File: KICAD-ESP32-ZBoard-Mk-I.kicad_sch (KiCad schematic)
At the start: 33 parts, among them J1 DC_Jack, J10 USB_A, J2 Conn_01x03_Pin-RAIL_1, J3 Conn_01x02_Pin-RAIL_1, J4 Conn_01x03_Pin-RAIL_2, J5 Conn_01x02_Pin-RAIL_2, J6 Conn_01x03_Pin-RAIL_3, J7 Conn_01x02_Pin-RAIL_3, J8 Conn_01x13_Pin-LEFT, J9 Conn_01x13_Pin-RIGHT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

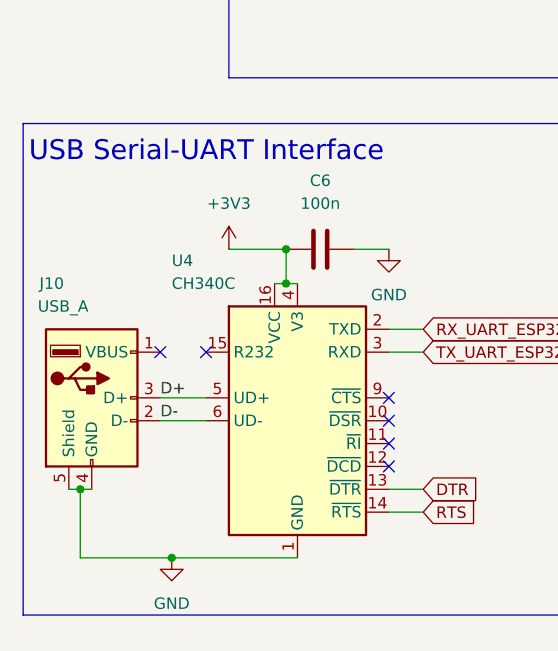
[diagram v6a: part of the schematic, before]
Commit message: ADDED all remaining pin labels. ADDED serial-breakout pins in case alternative USB is wanted.
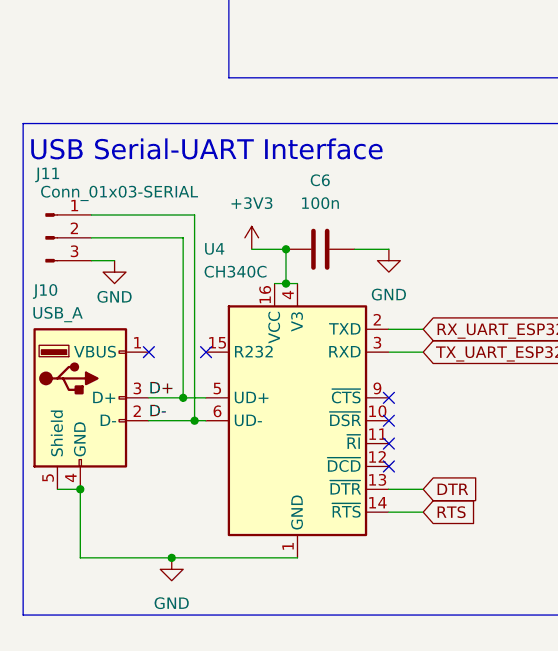
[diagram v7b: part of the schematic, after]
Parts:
- added J11: Conn_01x03-SERIAL, Connector_PinHeader_2.54mm:PinHeader_1x03_P2.54mm_Vertical, symbol Connector:Conn_01x03_Pin
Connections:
- net D+: now also J11.2 (Pin_2)
- net D-: now also J11.1 (Pin_1)
- net GND: now also J11.3 (Pin_3)
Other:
- moved on the sheet: J10
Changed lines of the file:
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@@
 	)
 	(junction
+		(at 34.29 151.13)
+		(diameter 0)
+		(color 0 0 0 0)
+	)
+	(junction
 		(at 66.04 87.63)
 		(diameter 0)
@@
 	)
 	(junction
+		(at 33.02 148.59)
+		(diameter 0)
+		(color 0 0 0 0)
+	)
+	(junction
 		(at 134.62 39.37)
 		(diameter 0)
@@
 	)
 	(no_connect
-		(at 30.48 143.51)
+		(at 29.21 143.51)
 	)
 	(no_connect
@@
 	(wire
 		(pts
-			(xy 21.59 158.75) (xy 20.32 158.75)
+			(xy 21.59 158.75) (xy 19.05 158.75)
 		)
 		(stroke
@@
 	(wire
 		(pts
+			(xy 29.21 151.13) (xy 34.29 151.13)
+		)
+		(stroke
+			(width 0)
+			(type default)
+		)
+	)
+	(wire
+		(pts
 			(xy 154.94 156.21) (xy 158.75 156.21)
 		)
@@
 	(wire
 		(pts
+			(xy 22.86 130.81) (xy 33.02 130.81)
+		)
+		(stroke
+			(width 0)
+			(type default)
+		)
+	)
+	(wire
+		(pts
 			(xy 186.69 158.75) (xy 190.5 158.75)
 		)
@@
 	(wire
 		(pts
-			(xy 93.98 33.02) (xy 105.41 33.02)
+			(xy 34.29 128.27) (xy 34.29 151.13)
 		)
 		(stroke
@@
 	(wire
 		(pts
-			(xy 30.48 151.13) (xy 35.56 151.13)
+			(xy 93.98 33.02) (xy 105.41 33.02)
 		)
 		(stroke
@@
 	(wire
 		(pts
-			(xy 38.1 132.08) (xy 44.45 132.08)
+			(xy 40.64 132.08) (xy 44.45 132.08)
 		)
 		(stroke
@@
 	(wire
 		(pts
-			(xy 22.86 158.75) (xy 21.59 158.75)
-		)
-		(stroke
-			(width 0)
-			(type default)
-		)
-	)
-	(wire
-		(pts
 			(xy 95.25 137.16) (xy 96.52 137.16)
 		)
@@
 	(wire
 		(pts
-			(xy 30.48 148.59) (xy 35.56 148.59)
+			(xy 29.21 148.59) (xy 33.02 148.59)
 		)
 		(stroke
@@
 	(wire
 		(pts
+			(xy 33.02 148.59) (xy 35.56 148.59)
+		)
+		(stroke
+			(width 0)
+			(type default)
+		)
+	)
+	(wire
+		(pts
 			(xy 52.07 132.08) (xy 55.88 132.08)
 		)
@@
 	(wire
 		(pts
+			(xy 34.29 151.13) (xy 35.56 151.13)
+		)
+		(stroke
+			(width 0)
+			(type default)
+		)
+	)
+	(wire
+		(pts
 			(xy 154.94 135.89) (xy 158.75 135.89)
 		)
@@
 	(wire
 		(pts
+			(xy 33.02 130.81) (xy 33.02 148.59)
+		)
+		(stroke
+			(width 0)
+			(type default)
+		)
+	)
+	(wire
+		(pts
 			(xy 186.69 161.29) (xy 190.5 161.29)
 		)
@@
 	(wire
 		(pts
+			(xy 22.86 128.27) (xy 34.29 128.27)
+		)
+		(stroke
+			(width 0)
+			(type default)
+		)
+	)
+	(wire
+		(pts
 			(xy 39.37 36.83) (xy 39.37 33.02)
 		)
@@
 	(wire
 		(pts
+			(xy 22.86 133.35) (xy 25.4 133.35)
+		)
+		(stroke
+			(width 0)
+			(type default)
+		)
+	)
+	(wire
+		(pts
 			(xy 66.04 99.06) (xy 58.42 99.06)
 		)
@@
 	)
 	(label "D-"
-		(at 30.48 151.13 0)
+		(at 29.21 151.13 0)
 		(effects
 			(font
@@
 	)
 	(label "D+"
-		(at 30.48 148.59 0)
+		(at 29.21 148.59 0)
 		(effects
 			(font
@@
 	(symbol
 		(lib_id "power:+3V3")
-		(at 38.1 132.08 0)
+		(at 40.64 132.08 0)
 		(unit 1)
 		(exclude_from_sim no)
@@
 		(fields_autoplaced yes)
 		(property "Reference" "#PWR013"
-			(at 38.1 135.89 0)
+			(at 40.64 135.89 0)
 			(effects
 				(font
@@
 		)
 		(property "Value" "+3V3"
-			(at 38.1 127 0)
+			(at 40.64 127 0)
 			(effects
 				(font
@@
 		)
 		(property "Footprint" ""
-			(at 38.1 132.08 0)
+			(at 40.64 132.08 0)
 			(effects
 				(font
@@
 		)
 		(property "Datasheet" ""
-			(at 38.1 132.08 0)
+			(at 40.64 132.08 0)
 			(effects
 				(font
@@
 		)
 		(property "Description" "Power symbol creates a global label with name \"+3V3\""
-			(at 38.1 132.08 0)
+			(at 40.64 132.08 0)
 			(effects
 				(font
@@
 	(symbol
 		(lib_id "Connector:Conn_01x03_Pin")
+		(at 17.78 130.81 0)
+		(unit 1)
+		(exclude_from_sim no)
+		(in_bom yes)
+		(on_board yes)
+		(dnp no)
+		(property "Reference" "J11"
+			(at 18.034 123.698 0)
+			(effects
+				(font
+					(size 1.27 1.27)
+				)
+			)
+		)
+		(property "Value" "Conn_01x03-SERIAL"
+			(at 25.908 125.73 0)
+			(effects
+				(font
+					(size 1.27 1.27)
+				)
+			)
+		)
+		(property "Footprint" "Connector_PinHeader_2.54mm:PinHeader_1x03_P2.54mm_Vertical"
+			(at 17.78 130.81 0)
+			(effects
+				(font
+					(size 1.27 1.27)
+				)
+				(hide yes)
+			)
+		)
+		(property "Datasheet" "~"
+			(at 17.78 130.81 0)
+			(effects
+				(font
+					(size 1.27 1.27)
+				)
+				(hide yes)
+			)
+		)
+		(property "Description" "Generic connector, single row, 01x03, script generated"
+			(at 17.78 130.81 0)
+			(effects
+				(font
+					(size 1.27 1.27)
+				)
+				(hide yes)
+			)
+		)
+		(pin "1"
+		)
+		(pin "2"
+		)
+		(pin "3"
+		)
+		(instances
+			(project ""
+				(path "/5468ddea-f4b3-4e6a-b463-e1f542c63303"
+					(reference "J11")
+					(unit 1)
+				)
+			)
+		)
+	)
+	(symbol
+		(lib_id "Connector:Conn_01x03_Pin")
 		(at 53.34 101.6 0)
 		(unit 1)
@@
 		(dnp no)
 		(property "Reference" "U4"
-			(at 31.75 133.35 0)
+			(at 35.306 132.08 0)
 			(effects
 				(font
@@
 		)
 		(property "Value" "CH340C"
-			(at 31.75 135.89 0)
+			(at 35.306 134.62 0)
 			(effects
 				(font
@@
 	)
 	(symbol
+		(lib_id "power:GND")
+		(at 25.4 133.35 0)
+		(unit 1)
+		(exclude_from_sim no)
+		(in_bom yes)
+		(on_board yes)
+		(dnp no)
+		(property "Reference" "#PWR018"
+			(at 25.4 139.7 0)
+			(effects
+				(font
+					(size 1.27 1.27)
+				)
+				(hide yes)
+			)
+		)
+		(property "Value" "GND"
+			(at 25.4 137.414 0)
+			(effects
+				(font
+					(size 1.27 1.27)
+				)
+			)
+		)
+		(property "Footprint" ""
+			(at 25.4 133.35 0)
+			(effects
+				(font
+					(size 1.27 1.27)
+				)
+				(hide yes)
+			)
+		)
+		(property "Datasheet" ""
+			(at 25.4 133.35 0)
+			(effects
+				(font
+					(size 1.27 1.27)
+				)
+				(hide yes)
+			)
+		)
+		(property "Description" "Power symbol creates a global label with name \"GND\" , ground"
+			(at 25.4 133.35 0)
+			(effects
+				(font
+					(size 1.27 1.27)
+				)
+				(hide yes)
+			)
+		)
+		(pin "1"
+		)
+		(instances
+			(project "KICAD-ESP32-ZBoard-Mk-I"
+				(path "/5468ddea-f4b3-4e6a-b463-e1f542c63303"
+					(reference "#PWR018")
+					(unit 1)
+				)
+			)
+		)
+	)
+	(symbol
 		(lib_id "Switch:SW_Push")
 		(at 129.54 39.37 0)
@@
 	(symbol
 		(lib_id "Connector:USB_A")
-		(at 22.86 148.59 0)
+		(at 21.59 148.59 0)
 		(unit 1)
 		(exclude_from_sim no)
@@
 		(dnp no)
 		(property "Reference" "J10"
-			(at 18.415 135.89 0)
+			(at 17.78 136.652 0)
 			(effects
 				(font
@@
 		)
 		(property "Value" "USB_A"
-			(at 19.685 138.43 0)
+			(at 19.05 139.192 0)
 			(effects
 				(font
@@
 		)
 		(property "Footprint" "ZCustomFootprints:USB-A Jing (C42576)"
-			(at 26.67 149.86 0)
+			(at 25.4 149.86 0)
 			(effects
 				(font
@@
 		)
 		(property "Datasheet" "~"
-			(at 26.67 149.86 0)
+			(at 25.4 149.86 0)
 			(effects
 				(font
@@
 		)
 		(property "Description" "USB Type A connector"
-			(at 22.86 148.59 0)
+			(at 21.59 148.59 0)
 			(effects
 				(font
@@
 		)
 		(property "LCSC Part #" "C42576"
-			(at 22.86 148.59 0)
+			(at 21.59 148.59 0)
 			(effects
 				(font

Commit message: Generated BOM for assembly
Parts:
- J11: LCSC Part # (none) -> n/a
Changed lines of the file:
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@@
+			)
+		)
+		(property "LCSC Part #" "n/a"
+			(at 17.78 130.81 0)
+			(effects
+				(font
+					(size 1.27 1.27)
+				)
+				(hide yes)
 			)
 		)
